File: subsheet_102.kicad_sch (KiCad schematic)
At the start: 24 parts

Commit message: update comments in cartridge
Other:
- title: Conversion du Thomson MO5 — Unité centrale v1 -> Conversion du Thomson MO5 — Unité centrale v2
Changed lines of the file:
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@@
   (paper "A4" portrait)
   (title_block
-    (title "Conversion du Thomson MO5 — Unité centrale v1")
-    (date "2024-12-30")
-    (rev "v1.0.0-rc2")
+    (title "Conversion du Thomson MO5 — Unité centrale v2")
+    (date "2025-02-08")
+    (rev "v2.0.0-alpha")
     (comment 1 "http://github.com/sporniket/kicad-conversions--thomson-mo5--v1")
-    (comment 3 "Gate Array Motorola MCA 1300 ALS")
-    (comment 4 "Reference : POP5001 501994-01")
+    (comment 3 "Gate Array EFCIS")
   )
   (junction (at 90.17 193.04) (diameter 0) (color 0 0 0 0)

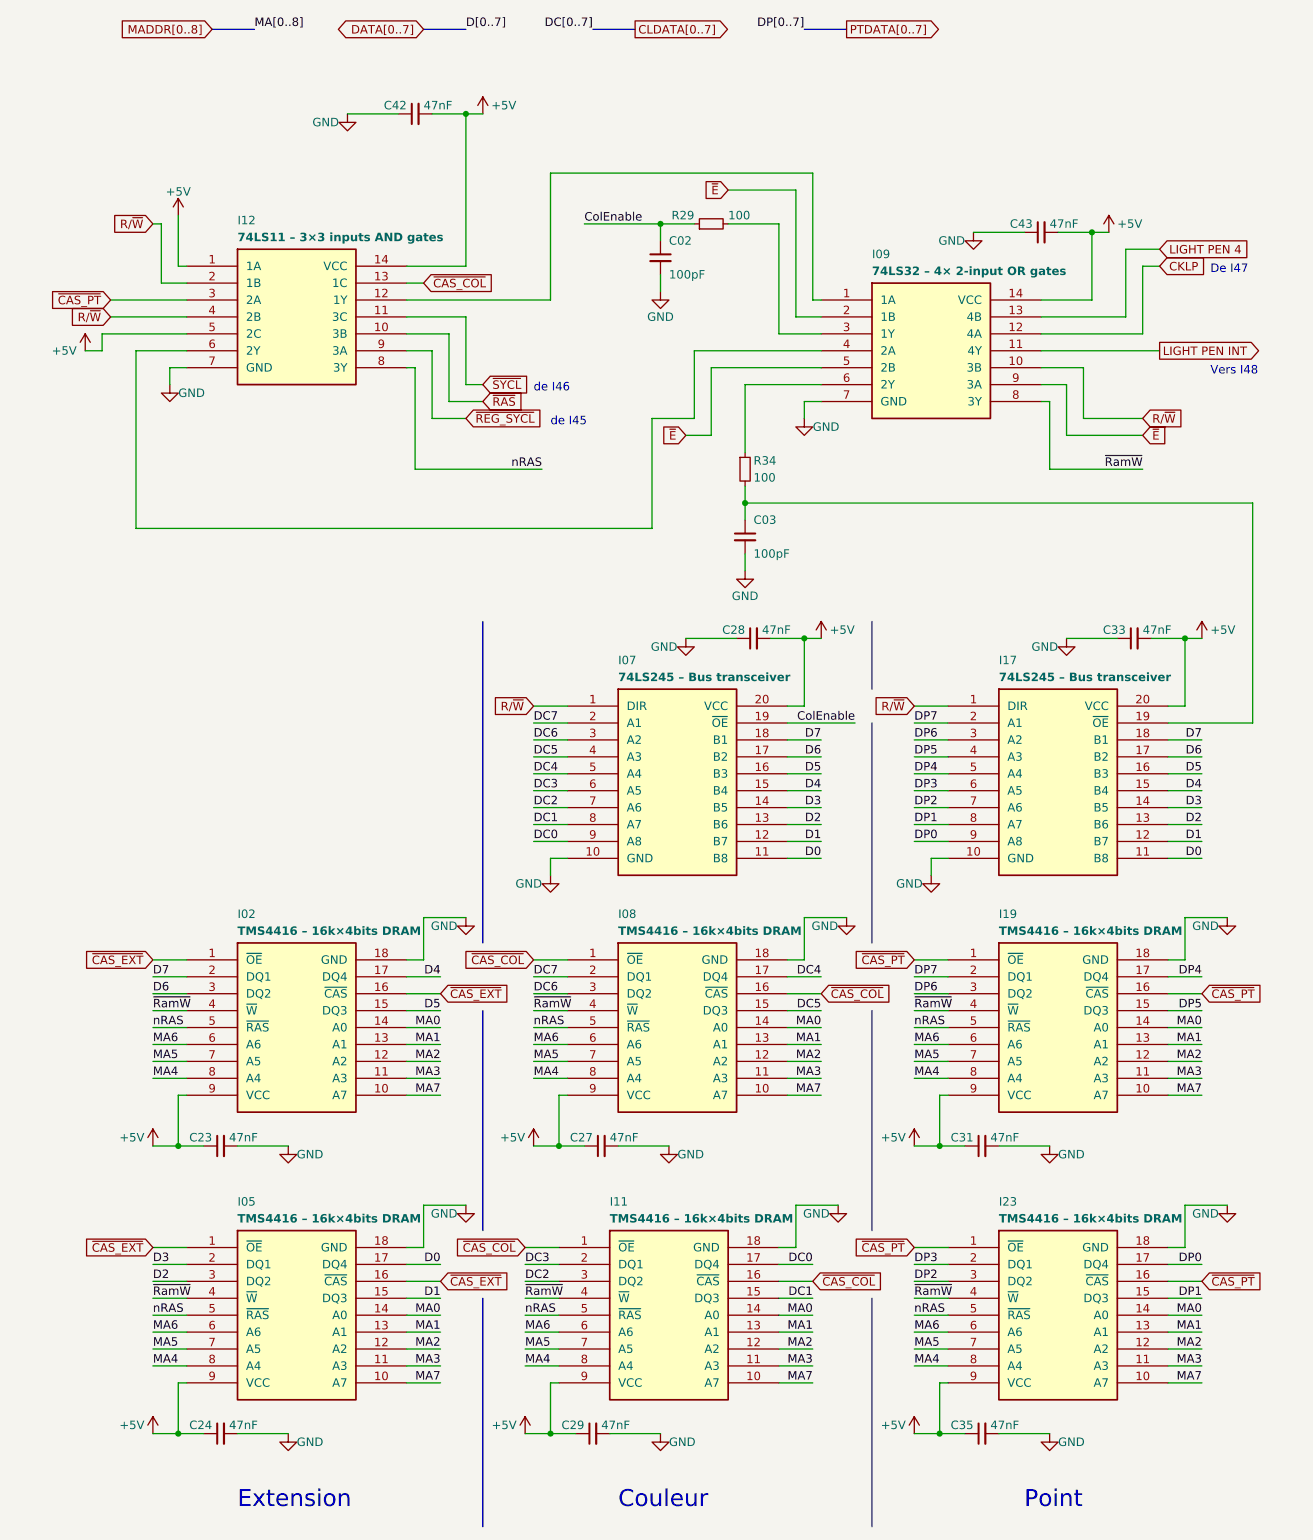
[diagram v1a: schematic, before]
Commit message: Resolves #15 : [ga efcis] SIPP memory modules I100 I101 I102
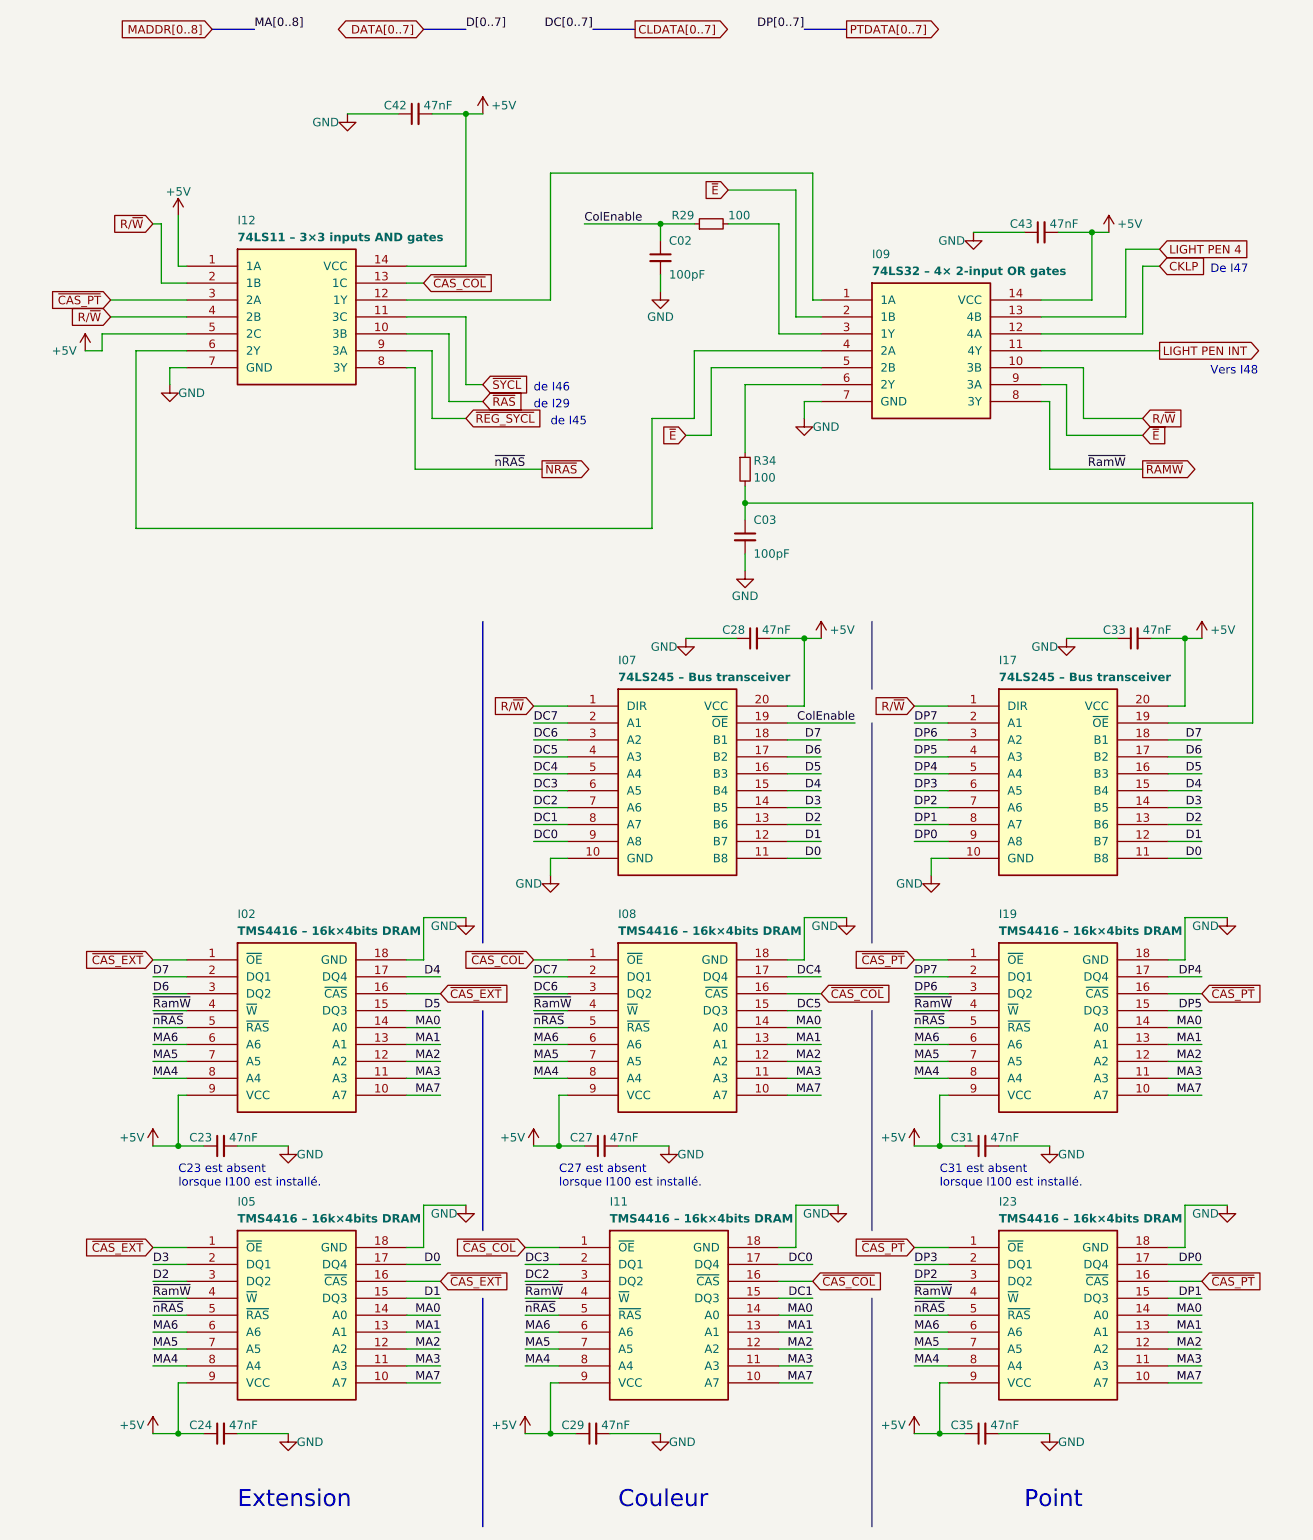
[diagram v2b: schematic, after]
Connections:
- net nRAS renamed ~{NRAS}
- net ~{RamW} renamed ~{RAMW}
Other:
- note added: "C23 est absent lorsque I100 est installé."
- note added: "C27 est absent lorsque I100 est installé."
- note added: "C31 est absent lorsque I100 est installé."
- note added: "de I29"
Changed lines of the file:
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@@
     (stroke (width 0) (type default))
+  )
+  (text "C31 est absent\nlorsque I100 est installé." (at 147.32 199.39 0)
+    (effects (font (size 1.27 1.27)) (justify left bottom))
+  )
+  (text "de I29" (at 86.36 82.55 0)
+    (effects (font (size 1.27 1.27)) (justify left bottom))
   )
   (text "Extension" (at 41.91 247.65 0)
@@
     (effects (font (size 1.27 1.27)) (justify left bottom))
   )
+  (text "C27 est absent\nlorsque I100 est installé." (at 90.17 199.39 0)
+    (effects (font (size 1.27 1.27)) (justify left bottom))
+  )
   (text "de I45" (at 88.9 85.09 0)
+    (effects (font (size 1.27 1.27)) (justify left bottom))
+  )
+  (text "C23 est absent\nlorsque I100 est installé." (at 33.02 199.39 0)
     (effects (font (size 1.27 1.27)) (justify left bottom))
   )
@@
     (effects (font (size 2.54 2.54)) (justify left bottom))
   )
-  (label "nRAS" (at 29.21 175.26 0) (fields_autoplaced)
-    (effects (font (size 1.27 1.27)) (justify left bottom))
-  )
-  (label "nRAS" (at 86.36 175.26 0) (fields_autoplaced)
+  (label "~{nRAS}" (at 29.21 175.26 0) (fields_autoplaced)
+    (effects (font (size 1.27 1.27)) (justify left bottom))
+  )
+  (label "~{nRAS}" (at 86.36 175.26 0) (fields_autoplaced)
     (effects (font (size 1.27 1.27)) (justify left bottom))
   )
@@
     (effects (font (size 1.27 1.27)) (justify left bottom))
   )
-  (label "nRAS" (at 87.63 91.44 180) (fields_autoplaced)
+  (label "~{nRAS}" (at 85.09 91.44 180) (fields_autoplaced)
     (effects (font (size 1.27 1.27)) (justify right bottom))
   )
@@
     (effects (font (size 1.27 1.27)) (justify left bottom))
   )
-  (label "nRAS" (at 143.51 175.26 0) (fields_autoplaced)
+  (label "~{nRAS}" (at 143.51 175.26 0) (fields_autoplaced)
     (effects (font (size 1.27 1.27)) (justify left bottom))
   )
@@
     (effects (font (size 1.27 1.27)) (justify right bottom))
   )
-  (label "nRAS" (at 85.09 218.44 0) (fields_autoplaced)
+  (label "~{nRAS}" (at 85.09 218.44 0) (fields_autoplaced)
     (effects (font (size 1.27 1.27)) (justify left bottom))
   )
@@
     (effects (font (size 1.27 1.27)) (justify left bottom))
   )
-  (label "nRAS" (at 29.21 218.44 0) (fields_autoplaced)
+  (label "~{nRAS}" (at 29.21 218.44 0) (fields_autoplaced)
     (effects (font (size 1.27 1.27)) (justify left bottom))
   )
@@
     (effects (font (size 1.27 1.27)) (justify right bottom))
   )
-  (label "nRAS" (at 143.51 218.44 0) (fields_autoplaced)
+  (label "~{nRAS}" (at 143.51 218.44 0) (fields_autoplaced)
     (effects (font (size 1.27 1.27)) (justify left bottom))
   )
@@
     (effects (font (size 1.27 1.27)) (justify right bottom))
   )
-  (label "~{RamW}" (at 177.8 91.44 180) (fields_autoplaced)
+  (label "~{RamW}" (at 175.26 91.44 180) (fields_autoplaced)
     (effects (font (size 1.27 1.27)) (justify right bottom))
   )
@@
     )
   )
+  (global_label "~{NRAS}" (shape output) (at 87.63 91.44 0) (fields_autoplaced)
+    (effects (font (size 1.27 1.27)) (justify left))
+    (property "Intersheetrefs" "${INTERSHEET_REFS}" (at 95.5138 91.44 0)
+      (effects (font (size 1.27 1.27)) (justify left) hide)
+    )
+  )
   (global_label "~{CAS_PT}" (shape input) (at 186.69 213.36 0) (fields_autoplaced)
     (effects (font (size 1.27 1.27)) (justify left))
@@
       (effects (font (size 1.27 1.27)) (justify left) hide)
     )
+  )
+  (global_label "~{RAMW}" (shape output) (at 177.8 91.44 0) (fields_autoplaced)
+    (effects (font (size 1.27 1.27)) (justify left))
+    (property "Intersheetrefs" "${INTERSHEET_REFS}" (at 186.0466 91.44 0)
+      (effects (font (size 1.27 1.27)) (justify left) hide)
+    )
